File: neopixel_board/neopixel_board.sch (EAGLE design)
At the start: 64 parts, among them U1 UA7805CKCT, U2 MIC5219, U3 ATMEGA32U4, U4 UA7805CKCT, U5 UA7805CKCT, U6 UA7805CKCT, Y1 16MHz

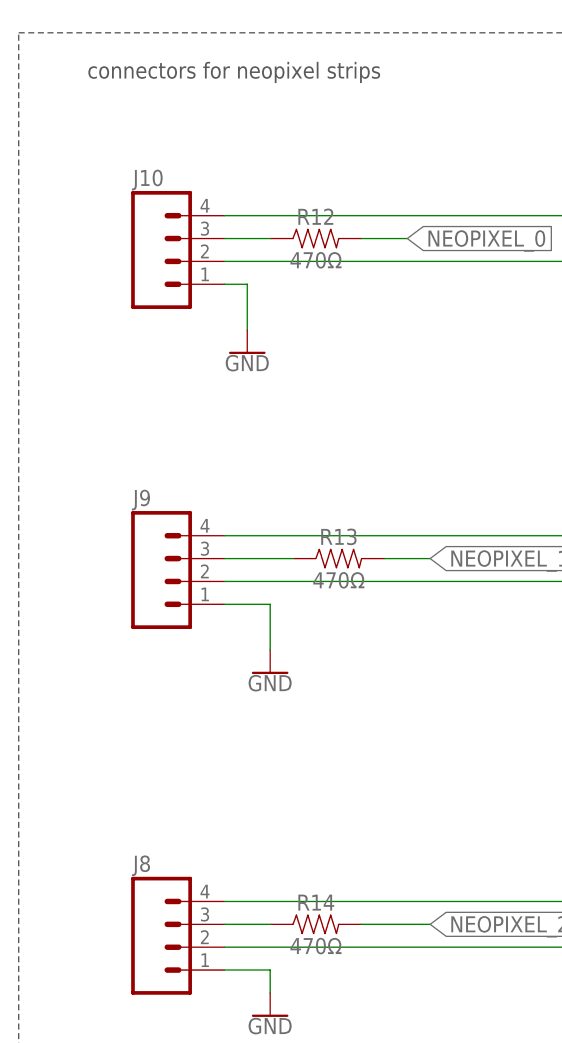
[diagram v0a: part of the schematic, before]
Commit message: Schematic changes
Named neopixel connectors in order
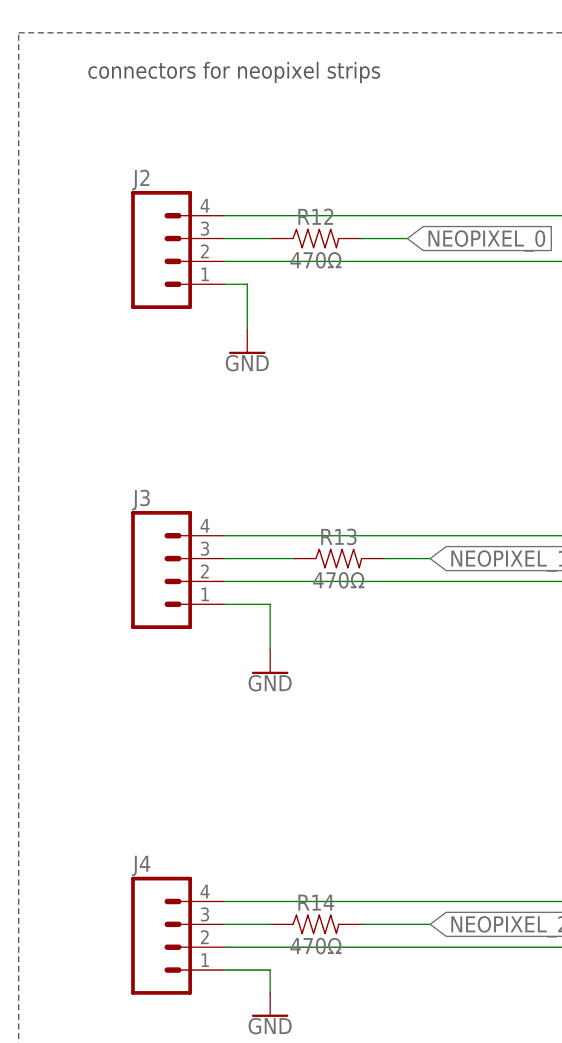
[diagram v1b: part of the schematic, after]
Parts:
- renumbered J10 to J2, J8 to J4, J9 to J3
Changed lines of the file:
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@@
 <part name="C16" library="rcl" library_urn="urn:adsk.eagle:library:334" deviceset="C-US" device="C0603" package3d_urn="urn:adsk.eagle:package:23616/2" value="0.1 uF"/>
 <part name="C17" library="rcl" library_urn="urn:adsk.eagle:library:334" deviceset="C-US" device="C0603" package3d_urn="urn:adsk.eagle:package:23616/2" value="0.33 uF"/>
-<part name="J8" library="SparkFun-Connectors" deviceset="M04" device="PTH"/>
-<part name="J9" library="SparkFun-Connectors" deviceset="M04" device="PTH"/>
-<part name="J10" library="SparkFun-Connectors" deviceset="M04" device="PTH"/>
+<part name="J4" library="SparkFun-Connectors" deviceset="M04" device="PTH"/>
+<part name="J3" library="SparkFun-Connectors" deviceset="M04" device="PTH"/>
+<part name="J2" library="SparkFun-Connectors" deviceset="M04" device="PTH"/>
 <part name="R12" library="SparkFun-Resistors" library_urn="urn:adsk.eagle:library:532" deviceset="470OHM" device="-0603-1/10W-1%" package3d_urn="urn:adsk.eagle:package:39650/1" value="470Ω"/>
 <part name="R13" library="SparkFun-Resistors" library_urn="urn:adsk.eagle:library:532" deviceset="470OHM" device="-0603-1/10W-1%" package3d_urn="urn:adsk.eagle:package:39650/1" value="470Ω"/>
@@
 <attribute name="VALUE" x="-69.469" y="69.596" size="1.778" layer="96" rot="R90"/>
 </instance>
-<instance part="J8" gate="G$1" x="-220.98" y="71.12">
+<instance part="J4" gate="G$1" x="-220.98" y="71.12">
 <attribute name="VALUE" x="-226.06" y="63.5" size="1.778" layer="96"/>
 <attribute name="NAME" x="-226.06" y="79.502" size="1.778" layer="95"/>
 </instance>
-<instance part="J9" gate="G$1" x="-220.98" y="111.76">
+<instance part="J3" gate="G$1" x="-220.98" y="111.76">
 <attribute name="VALUE" x="-226.06" y="104.14" size="1.778" layer="96"/>
 <attribute name="NAME" x="-226.06" y="120.142" size="1.778" layer="95"/>
 </instance>
-<instance part="J10" gate="G$1" x="-220.98" y="147.32">
+<instance part="J2" gate="G$1" x="-220.98" y="147.32">
 <attribute name="VALUE" x="-226.06" y="139.7" size="1.778" layer="96"/>
 <attribute name="NAME" x="-226.06" y="155.702" size="1.778" layer="95"/>
@@
 </segment>
 <segment>
-<pinref part="J10" gate="G$1" pin="1"/>
+<pinref part="J2" gate="G$1" pin="1"/>
 <wire x1="-215.9" y1="144.78" x2="-213.36" y2="144.78" width="0.1524" layer="91"/>
 <wire x1="-213.36" y1="144.78" x2="-213.36" y2="139.7" width="0.1524" layer="91"/>
@@
 </segment>
 <segment>
-<pinref part="J8" gate="G$1" pin="2"/>
+<pinref part="J4" gate="G$1" pin="2"/>
 <wire x1="-215.9" y1="71.12" x2="-175.26" y2="71.12" width="0.1524" layer="91"/>
 <wire x1="-175.26" y1="71.12" x2="-175.26" y2="68.58" width="0.1524" layer="91"/>
@@
 </segment>
 <segment>
-<pinref part="J10" gate="G$1" pin="2"/>
+<pinref part="J2" gate="G$1" pin="2"/>
 <wire x1="-215.9" y1="147.32" x2="-170.18" y2="147.32" width="0.1524" layer="91"/>
 <wire x1="-170.18" y1="147.32" x2="-170.18" y2="144.78" width="0.1524" layer="91"/>
@@
 <segment>
 <wire x1="-167.64" y1="109.22" x2="-167.64" y2="106.68" width="0.1524" layer="91"/>
-<pinref part="J9" gate="G$1" pin="2"/>
+<pinref part="J3" gate="G$1" pin="2"/>
 <wire x1="-215.9" y1="111.76" x2="-170.18" y2="111.76" width="0.1524" layer="91"/>
 <wire x1="-170.18" y1="111.76" x2="-170.18" y2="109.22" width="0.1524" layer="91"/>
@@
 </segment>
 <segment>
-<pinref part="J9" gate="G$1" pin="1"/>
+<pinref part="J3" gate="G$1" pin="1"/>
 <wire x1="-215.9" y1="109.22" x2="-210.82" y2="109.22" width="0.1524" layer="91"/>
 <wire x1="-210.82" y1="109.22" x2="-210.82" y2="104.14" width="0.1524" layer="91"/>
@@
 </segment>
 <segment>
-<pinref part="J8" gate="G$1" pin="1"/>
+<pinref part="J4" gate="G$1" pin="1"/>
 <wire x1="-215.9" y1="68.58" x2="-210.82" y2="68.58" width="0.1524" layer="91"/>
 <wire x1="-210.82" y1="68.58" x2="-210.82" y2="66.04" width="0.1524" layer="91"/>
@@
 <net name="VCC2" class="0">
 <segment>
-<pinref part="J10" gate="G$1" pin="4"/>
+<pinref part="J2" gate="G$1" pin="4"/>
 <wire x1="-215.9" y1="152.4" x2="-167.64" y2="152.4" width="0.1524" layer="91"/>
 <label x="-160.02" y="152.4" size="1.778" layer="95" xref="yes"/>
@@
 </segment>
 <segment>
-<pinref part="J9" gate="G$1" pin="4"/>
+<pinref part="J3" gate="G$1" pin="4"/>
 <wire x1="-215.9" y1="116.84" x2="-167.64" y2="116.84" width="0.1524" layer="91"/>
 <label x="-160.02" y="116.84" size="1.778" layer="95" xref="yes"/>
@@
 <net name="VCC4" class="0">
 <segment>
-<pinref part="J8" gate="G$1" pin="4"/>
+<pinref part="J4" gate="G$1" pin="4"/>
 <wire x1="-215.9" y1="76.2" x2="-172.72" y2="76.2" width="0.1524" layer="91"/>
 <label x="-165.1" y="76.2" size="1.778" layer="95" xref="yes"/>
@@
 <pinref part="R12" gate="G$1" pin="1"/>
 <wire x1="-215.9" y1="149.86" x2="-210.82" y2="149.86" width="0.1524" layer="91"/>
-<pinref part="J10" gate="G$1" pin="3"/>
+<pinref part="J2" gate="G$1" pin="3"/>
 </segment>
 </net>
@@
 <segment>
 <pinref part="R13" gate="G$1" pin="1"/>
-<pinref part="J9" gate="G$1" pin="3"/>
+<pinref part="J3" gate="G$1" pin="3"/>
 <wire x1="-215.9" y1="114.3" x2="-208.28" y2="114.3" width="0.1524" layer="91"/>
 </segment>
@@
 <segment>
 <pinref part="R14" gate="G$1" pin="1"/>
-<pinref part="J8" gate="G$1" pin="3"/>
+<pinref part="J4" gate="G$1" pin="3"/>
 <wire x1="-210.82" y1="73.66" x2="-215.9" y2="73.66" width="0.1524" layer="91"/>
 </segment>

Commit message: Schematic changes
-named connectors in order
-named VCC voltages
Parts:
- renumbered J2 to J10, J3 to J9, J4 to J8
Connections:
- net VCC1 renamed VCC1_5V
- net VCC2 renamed VCC2_5V
- net VCC3 renamed VCC3_5V
- net VCC4 renamed VCC4_5V
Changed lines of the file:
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@@
 <part name="C16" library="rcl" library_urn="urn:adsk.eagle:library:334" deviceset="C-US" device="C0603" package3d_urn="urn:adsk.eagle:package:23616/2" value="0.1 uF"/>
 <part name="C17" library="rcl" library_urn="urn:adsk.eagle:library:334" deviceset="C-US" device="C0603" package3d_urn="urn:adsk.eagle:package:23616/2" value="0.33 uF"/>
-<part name="J4" library="SparkFun-Connectors" deviceset="M04" device="PTH"/>
-<part name="J3" library="SparkFun-Connectors" deviceset="M04" device="PTH"/>
-<part name="J2" library="SparkFun-Connectors" deviceset="M04" device="PTH"/>
+<part name="J8" library="SparkFun-Connectors" deviceset="M04" device="PTH"/>
+<part name="J9" library="SparkFun-Connectors" deviceset="M04" device="PTH"/>
+<part name="J10" library="SparkFun-Connectors" deviceset="M04" device="PTH"/>
 <part name="R12" library="SparkFun-Resistors" library_urn="urn:adsk.eagle:library:532" deviceset="470OHM" device="-0603-1/10W-1%" package3d_urn="urn:adsk.eagle:package:39650/1" value="470Ω"/>
 <part name="R13" library="SparkFun-Resistors" library_urn="urn:adsk.eagle:library:532" deviceset="470OHM" device="-0603-1/10W-1%" package3d_urn="urn:adsk.eagle:package:39650/1" value="470Ω"/>
@@
 <text x="40.64" y="71.12" size="1.778" layer="97">Max Current Output: 500mA</text>
 <text x="40.64" y="68.58" size="1.778" layer="97">Board is marked with combination of</text>
-<text x="35.56" y="66.04" size="1.778" layer="97">resonator frequency and regulator voltage.</text>
+<text x="40.64" y="66.04" size="1.778" layer="97">resonator frequency and regulator voltage.</text>
 <text x="40.64" y="76.2" size="1.778" layer="97">VCC = 3.3V Output</text>
 <wire x1="17.78" y1="-5.08" x2="17.78" y2="-38.1" width="0.1524" layer="97" style="longdash"/>
@@
 <wire x1="119.38" y1="-12.7" x2="119.38" y2="121.92" width="0.1524" layer="97" style="longdash"/>
 <text x="121.92" y="116.84" size="1.778" layer="97">ATMega</text>
-<wire x1="-238.76" y1="172.72" x2="-149.86" y2="172.72" width="0.1524" layer="97" style="longdash"/>
-<wire x1="-149.86" y1="172.72" x2="-149.86" y2="40.64" width="0.1524" layer="97" style="longdash"/>
-<wire x1="-149.86" y1="40.64" x2="-238.76" y2="40.64" width="0.1524" layer="97" style="longdash"/>
+<wire x1="-238.76" y1="172.72" x2="-142.24" y2="172.72" width="0.1524" layer="97" style="longdash"/>
+<wire x1="-142.24" y1="172.72" x2="-142.24" y2="40.64" width="0.1524" layer="97" style="longdash"/>
+<wire x1="-142.24" y1="40.64" x2="-238.76" y2="40.64" width="0.1524" layer="97" style="longdash"/>
 <wire x1="-238.76" y1="40.64" x2="-238.76" y2="172.72" width="0.1524" layer="97" style="longdash"/>
 <text x="-231.14" y="167.64" size="1.778" layer="97">connectors for neopixel strips</text>
@@
 <attribute name="VALUE" x="-69.469" y="69.596" size="1.778" layer="96" rot="R90"/>
 </instance>
-<instance part="J4" gate="G$1" x="-220.98" y="71.12">
+<instance part="J8" gate="G$1" x="-220.98" y="71.12">
 <attribute name="VALUE" x="-226.06" y="63.5" size="1.778" layer="96"/>
 <attribute name="NAME" x="-226.06" y="79.502" size="1.778" layer="95"/>
 </instance>
-<instance part="J3" gate="G$1" x="-220.98" y="111.76">
+<instance part="J9" gate="G$1" x="-220.98" y="111.76">
 <attribute name="VALUE" x="-226.06" y="104.14" size="1.778" layer="96"/>
 <attribute name="NAME" x="-226.06" y="120.142" size="1.778" layer="95"/>
 </instance>
-<instance part="J2" gate="G$1" x="-220.98" y="147.32">
+<instance part="J10" gate="G$1" x="-220.98" y="147.32">
 <attribute name="VALUE" x="-226.06" y="139.7" size="1.778" layer="96"/>
 <attribute name="NAME" x="-226.06" y="155.702" size="1.778" layer="95"/>
@@
 </segment>
 <segment>
-<pinref part="J2" gate="G$1" pin="1"/>
+<pinref part="J10" gate="G$1" pin="1"/>
 <wire x1="-215.9" y1="144.78" x2="-213.36" y2="144.78" width="0.1524" layer="91"/>
 <wire x1="-213.36" y1="144.78" x2="-213.36" y2="139.7" width="0.1524" layer="91"/>
@@
 </segment>
 <segment>
-<pinref part="J4" gate="G$1" pin="2"/>
+<pinref part="J8" gate="G$1" pin="2"/>
 <wire x1="-215.9" y1="71.12" x2="-175.26" y2="71.12" width="0.1524" layer="91"/>
 <wire x1="-175.26" y1="71.12" x2="-175.26" y2="68.58" width="0.1524" layer="91"/>
@@
 </segment>
 <segment>
-<pinref part="J2" gate="G$1" pin="2"/>
+<pinref part="J10" gate="G$1" pin="2"/>
 <wire x1="-215.9" y1="147.32" x2="-170.18" y2="147.32" width="0.1524" layer="91"/>
 <wire x1="-170.18" y1="147.32" x2="-170.18" y2="144.78" width="0.1524" layer="91"/>
@@
 <segment>
 <wire x1="-167.64" y1="109.22" x2="-167.64" y2="106.68" width="0.1524" layer="91"/>
-<pinref part="J3" gate="G$1" pin="2"/>
+<pinref part="J9" gate="G$1" pin="2"/>
 <wire x1="-215.9" y1="111.76" x2="-170.18" y2="111.76" width="0.1524" layer="91"/>
 <wire x1="-170.18" y1="111.76" x2="-170.18" y2="109.22" width="0.1524" layer="91"/>
@@
 </segment>
 <segment>
-<pinref part="J3" gate="G$1" pin="1"/>
+<pinref part="J9" gate="G$1" pin="1"/>
 <wire x1="-215.9" y1="109.22" x2="-210.82" y2="109.22" width="0.1524" layer="91"/>
 <wire x1="-210.82" y1="109.22" x2="-210.82" y2="104.14" width="0.1524" layer="91"/>
@@
 </segment>
 <segment>
-<pinref part="J4" gate="G$1" pin="1"/>
+<pinref part="J8" gate="G$1" pin="1"/>
 <wire x1="-215.9" y1="68.58" x2="-210.82" y2="68.58" width="0.1524" layer="91"/>
 <wire x1="-210.82" y1="68.58" x2="-210.82" y2="66.04" width="0.1524" layer="91"/>
@@
 </segment>
 </net>
-<net name="VCC1" class="0">
+<net name="VCC1_5V" class="0">
 <segment>
 <pinref part="U1" gate="A" pin="OUT"/>
@@
 </segment>
 </net>
-<net name="VCC2" class="0">
-<segment>
-<pinref part="J2" gate="G$1" pin="4"/>
+<net name="VCC2_5V" class="0">
+<segment>
+<pinref part="J10" gate="G$1" pin="4"/>
 <wire x1="-215.9" y1="152.4" x2="-167.64" y2="152.4" width="0.1524" layer="91"/>
 <label x="-160.02" y="152.4" size="1.778" layer="95" xref="yes"/>
@@
 </segment>
 </net>
-<net name="VCC3" class="0">
+<net name="VCC3_5V" class="0">
 <segment>
 <pinref part="U5" gate="A" pin="OUT"/>
@@
 </segment>
 <segment>
-<pinref part="J3" gate="G$1" pin="4"/>
+<pinref part="J9" gate="G$1" pin="4"/>
 <wire x1="-215.9" y1="116.84" x2="-167.64" y2="116.84" width="0.1524" layer="91"/>
 <label x="-160.02" y="116.84" size="1.778" layer="95" xref="yes"/>
@@
 </segment>
 </net>
-<net name="VCC4" class="0">
-<segment>
-<pinref part="J4" gate="G$1" pin="4"/>
+<net name="VCC4_5V" class="0">
+<segment>
+<pinref part="J8" gate="G$1" pin="4"/>
 <wire x1="-215.9" y1="76.2" x2="-172.72" y2="76.2" width="0.1524" layer="91"/>
 <label x="-165.1" y="76.2" size="1.778" layer="95" xref="yes"/>
@@
 <pinref part="R12" gate="G$1" pin="1"/>
 <wire x1="-215.9" y1="149.86" x2="-210.82" y2="149.86" width="0.1524" layer="91"/>
-<pinref part="J2" gate="G$1" pin="3"/>
+<pinref part="J10" gate="G$1" pin="3"/>
 </segment>
 </net>
@@
 <segment>
 <pinref part="R13" gate="G$1" pin="1"/>
-<pinref part="J3" gate="G$1" pin="3"/>
+<pinref part="J9" gate="G$1" pin="3"/>
 <wire x1="-215.9" y1="114.3" x2="-208.28" y2="114.3" width="0.1524" layer="91"/>
 </segment>
@@
 <segment>
 <pinref part="R14" gate="G$1" pin="1"/>
-<pinref part="J4" gate="G$1" pin="3"/>
+<pinref part="J8" gate="G$1" pin="3"/>
 <wire x1="-210.82" y1="73.66" x2="-215.9" y2="73.66" width="0.1524" layer="91"/>
 </segment>

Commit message: Board Finished (tentative)
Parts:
- removed C1: 0.1uF, rcl:C-USC0603
- removed C11, C14, C16, C8: 0.1 uF, rcl:C-USC0603
- removed C15, C17, C9: 0.33 uF, rcl:C-USC0603
- removed C20, C21, C22: 1000uF, neopixel_board:UWT0J102MNL1GS
- removed J10, J8, J9: (no value), SparkFun-Connectors:M04PTH
- removed LD7: GREEN, SparkFun-LED:LED-GREEN0603
- removed R13, R14: 470Ω, SparkFun-Resistors:470OHM-0603-1/10W-1%
- removed R15: 1kΩ, SparkFun:RESISTOR0603-RES
- removed U1, U4, U5, U6: UA7805CKCT, Training_Board:UA7805CKCT
- removed U3: ATMEGA32U4, Testing:ATMEGA32U4OUTFAKES
- removed X1: (no value), Testing:USB-ABIN&OUT
- removed XF1: 4A, RoboJackets-Fuses:3557-2
- added 5VSOURCE, GND_TERMINAL: THOLE_SOURCE, neopixel_board:THOLE_SOURCE
- added F2, F3, F4: 4A, neopixel_board:3557-2
- added F5: 13A, neopixel_board:3557-2
- added J2, J3, J4: SSW-102-02-T-S-RA, neopixel_board:SSW-102-02-T-S-RA
- added J5: 47589-0001_2, neopixel_board:47589-0001_2
- added MCU: 32U4, SparkFun-IC-Microcontroller:ATMEGA32U4TQFP-44
- C12: value 0.33 uF -> 1000uF; device rcl:C-USC0603 -> SparkFun:CAP_POL1206
- J1: value (none) -> SSW-102-02-T-S-RA; device SparkFun-Connectors:CONN_023.5MM -> neopixel_board:SSW-102-02-T-S-RA
- R12: value 470Ω -> 1kΩ; device SparkFun-Resistors:470OHM-0603-1/10W-1% -> SparkFun:RESISTOR0603-RES
- R4: value 1kΩ -> 470Ω; device SparkFun:RESISTOR0603-RES -> SparkFun-Resistors:470OHM-0603-1/10W-1%
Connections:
- removed net AREF: C1.1, U3.AREF
- removed net N$3: J8.3, R14.1
- removed net NEOPIXEL_1: R13.2, U3.PB5(ADC12)
- removed net NEOPIXEL_2: R14.2, U3.PB6(ADC13)
- removed net UVCC: D1.A, X1.VBUS
- removed net VCC1_5V: C6.1, C9.1, F1.1, R15.1, U1.OUT, U3.UVCC, U3.VBUS
- removed net VCC2_5V: C12.1, C20.11, J10.4, R4.1, U4.OUT
- removed net VCC3_5V: C15.1, C21.11, J9.4, R9.1, U5.OUT
- removed net VCC4_5V: C17.1, C22.11, J8.4, R10.1, U6.OUT
- removed net VSOURCE: C11.1, C14.1, C16.1, C8.1, R3.2, U1.IN, U4.IN, U5.IN, U6.IN, XF1.2
- new net 5VIN: 5VSOURCE.1, F5.1
- new net N$17: D1.A, J5.1
- new net N$18: LD3.A, R2.2
- new net VCC_5V: C12.+, F1.1, F2.2, F3.2, F4.2, F5.2, R3.2
- net D+: now also MCU.D+; no longer U3.D+
- net D-: now also MCU.D-; no longer U3.D-
- net ETH_INT: now also MCU.PD7(ADC10); no longer U3.PD7(ADC10)
- net ETH_MISO: now also MCU.PB0(SS); no longer U3.PB3(MISO)
- net ETH_MOSI: now also MCU.PB2(MOSI); no longer U3.PB2(MOSI)
- net ETH_RST: now also MCU.PD2(RX); no longer U3.PD2(RX)
- net ETH_SCK: now also MCU.PB1(SCK); no longer U3.PB1(SCK)
- net ETH_SCNN: now also MCU.PB3(MISO); no longer U3.PB0(SS)
- net GND: now also C12.-, GND_TERMINAL.1, J2.1, J3.1, J4.1, J5.5, J5.SHIELD, MCU.AREF, MCU.GND@15, MCU.GND@23, MCU.GND@35, MCU.GND@43, MCU.PE2/!HWB, MCU.UGND; no longer C1.2, C11.2, C12.2, C14.2, C15.2, C16.2, C17.2, C20.22, C21.22, C22.22, C8.2, C9.2, J10.1, J10.2, J8.1, J8.2, J9.1, J9.2, LD3.A, LD7.C, R2.2, U1.COM, U3.GND@15, U3.GND@23, U3.GND@35, U3.GND@43, U3.PE2/!HWB, U3.UGND, U4.COM, U5.COM, U6.COM, X1.GND
- net MCU_RST: now also MCU.!RESET; no longer U3.!RESET
- net N$1: now also MCU.XTAL2; no longer U3.XTAL2
- net N$10: now also F2.1, J2.2, R9.2; no longer LD7.A, R10.2
- net N$11: now also F3.1, J1.2, R10.2; no longer LD4.A, R15.2
- net N$12: now also F4.1, J3.2, R12.2; no longer LD5.A, R4.2
- net N$13: now also J4.2, R4.1; no longer LD6.A, R9.2
- net N$14: now also LD4.A; no longer J10.3
- net N$15: now also LD5.A, R10.1; no longer J9.3, R13.1
- net N$16: now also LD6.A, R9.1; no longer J1.2, XF1.1
- net N$2: now also MCU.XTAL1; no longer U3.XTAL1
- net N$4: now also MCU.UCAP; no longer U3.UCAP
- net N$6: now also J5.2; no longer X1.D-
- net N$8: now also J5.3; no longer X1.D+
- net NEOPIXEL_0: now also MCU.PC6, R4.2; no longer R12.2, U3.PC6
- net TXLED: now also MCU.PD5; no longer U3.PD5
- net VCC1_3.3V: now also C6.1, MCU.AVCC@24, MCU.AVCC@44, MCU.UVCC, MCU.VBUS, MCU.VCC@14, MCU.VCC@34; no longer U3.AVCC@24, U3.AVCC@44, U3.VCC@14, U3.VCC@34
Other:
- note added: "DATA_CON"
- note added: "POWER_CON_1"
- note added: "POWER_CON_2"
- note added: "POWER_CON_3"
- note added: "Reset PB ATmega"
- note added: "Reset PB WIZNET"
- note added: "THROUGHHOLE TERMINAL (10AWG)"
- note added: "WIZNET Header"
- note removed: "Reset PB"
- note removed: "Screw terminals"
- note removed: "Voltage Regulators"
- note removed: "Wiznet Header"
- note removed: "change screw terminal to 5mm (14AWG)"
- note removed: "connectors for neopixel strips"
- note removed: "respec resistors on led and add led"
- moved on the sheet: C10, C13, C18, C19, C2, C3, C4, C5, C6, C7, D1, D2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

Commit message: BRD finishing touches
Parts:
- ETH1: device WIZ850io:WIZ850IO -> neopixel_board:WIZ850IO
- J5: value 47589-0001_2 -> 1981584-1; device neopixel_board:47589-0001_2 -> neopixel_board:1981584-1
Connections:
- net D+ renamed D_P
- net D- renamed D_N
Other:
- moved on the sheet: J5
